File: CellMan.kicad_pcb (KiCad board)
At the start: 2 copper layers, 99.1 x 45.7 mm, 61 parts, among them J1 Conn_01x05_Male, J2 IDC-Connector, J3 AVX-IDC, M1 SMT-Standoff, M2 SMT-Standoff, M3 SMT-Standoff, M4 SMT-Standoff, Q1 SP8K24FRATB, T1 FlybackTransformer, U1 L78L05CD13TR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

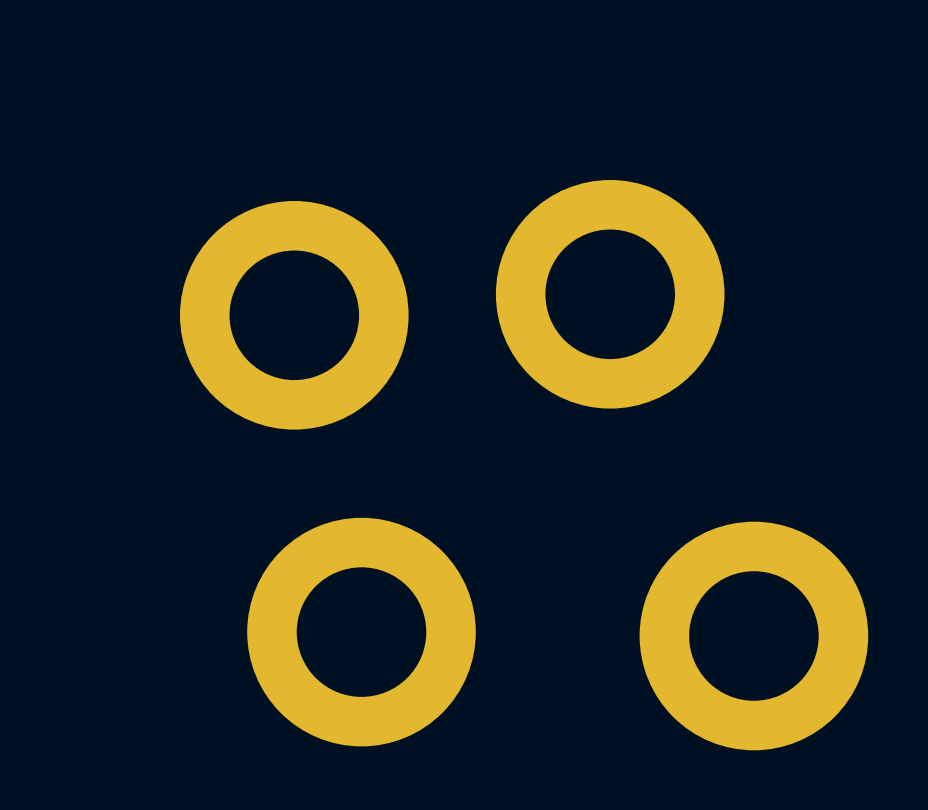
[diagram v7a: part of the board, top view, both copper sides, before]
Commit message: Removed Extra Mounting Holes
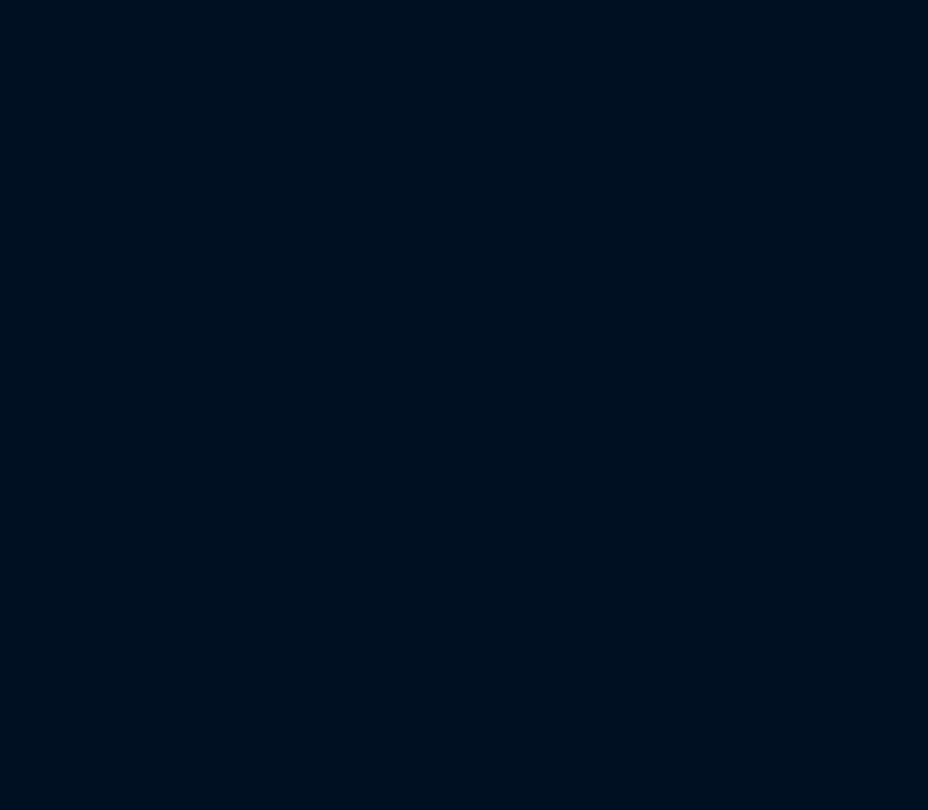
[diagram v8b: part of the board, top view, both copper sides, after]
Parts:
- removed M1, M2, M3, M4: SMT-Standoff, Lafayette_Electric_Car_Footprints:standoff_smt_4
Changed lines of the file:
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@@
     (tracks 505)
     (zones 0)
-    (modules 61)
+    (modules 57)
     (nets 42)
   )
@@
     (add_net "Net-(JP3-Pad1)")
     (add_net "Net-(JP3-Pad2)")
-    (add_net "Net-(M1-Pad1)")
-    (add_net "Net-(M2-Pad1)")
-    (add_net "Net-(M3-Pad1)")
-    (add_net "Net-(M4-Pad1)")
     (add_net "Net-(MCU1-Pad6)")
     (add_net "Net-(R14-Pad2)")
@@
     )
   )
-  (module Lafayette_Electric_Car_Footprints:standoff_smt_4 (layer F.Cu)
-    (at 191.64 151.28)
-    (fp_text reference M4 (at 5.88 -3.9) (layer F.SilkS) hide
-      (effects (font (size 1 1) (thickness 0.15)))
-    )
-    (fp_text value SMT-Standoff (at -0.28 -6.07) (layer F.Fab)
-      (effects (font (size 1 1) (thickness 0.15)))
-    )
-    (pad 1 thru_hole circle (at 0 0) (size 7.62 7.62) (drill 4.318) (layers *.Cu *.Mask))
-  )
-  (module Lafayette_Electric_Car_Footprints:standoff_smt_4 (layer F.Cu)
-    (at 181.11 151.98)
-    (fp_text reference M3 (at 5.88 -3.9) (layer F.SilkS) hide
-      (effects (font (size 1 1) (thickness 0.15)))
-    )
-    (fp_text value SMT-Standoff (at -0.28 -6.07) (layer F.Fab)
-      (effects (font (size 1 1) (thickness 0.15)))
-    )
-    (pad 1 thru_hole circle (at 0 0) (size 7.62 7.62) (drill 4.318) (layers *.Cu *.Mask))
-  )
-  (module Lafayette_Electric_Car_Footprints:standoff_smt_4 (layer F.Cu)
-    (at 183.35 162.54)
-    (fp_text reference M2 (at 5.88 -3.9) (layer F.SilkS) hide
-      (effects (font (size 1 1) (thickness 0.15)))
-    )
-    (fp_text value SMT-Standoff (at -0.28 -6.07) (layer F.Fab)
-      (effects (font (size 1 1) (thickness 0.15)))
-    )
-    (pad 1 thru_hole circle (at 0 0) (size 7.62 7.62) (drill 4.318) (layers *.Cu *.Mask))
-  )
-  (module Lafayette_Electric_Car_Footprints:standoff_smt_4 (layer F.Cu)
-    (at 196.43 162.67)
-    (fp_text reference M1 (at -2.39268 5.1562) (layer F.SilkS) hide
-      (effects (font (size 1 1) (thickness 0.15)))
-    )
-    (fp_text value SMT-Standoff (at -0.28 -6.07) (layer F.Fab)
-      (effects (font (size 1 1) (thickness 0.15)))
-    )
-    (pad 1 thru_hole circle (at 0 0) (size 7.62 7.62) (drill 4.318) (layers *.Cu *.Mask))
-  )
   (module Resistor_SMD:R_0805_2012Metric_Pad1.15x1.40mm_HandSolder (layer F.Cu)
